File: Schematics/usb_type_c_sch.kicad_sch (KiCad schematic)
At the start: 4 parts, among them J9 USB_C_Receptacle_USB2.0_16P

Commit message: added comments, awaiting review
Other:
- note added: "USB-C for flashing firmware"
- moved on the sheet: D4, J9, R13, R14

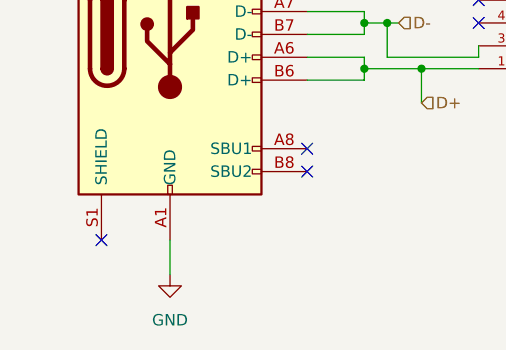
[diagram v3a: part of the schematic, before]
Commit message: fixed STLINK connector with correct pin mapping
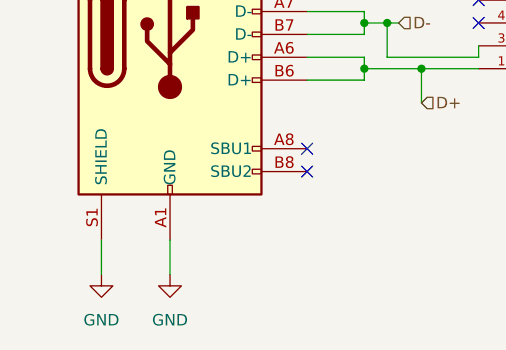
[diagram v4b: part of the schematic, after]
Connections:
- net GND: now also J9.S1 (SHIELD)
- no-connect marks 5 -> 4
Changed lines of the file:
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@@
-	)
-	(no_connect
-		(at 102.87 116.84)
 	)
 	(no_connect
@@
 		(pts
 			(xy 132.08 96.52) (xy 132.08 97.79)
+		)
+		(stroke
+			(width 0)
+			(type default)
+		)
+	)
+	(wire
+		(pts
+			(xy 102.87 120.65) (xy 102.87 116.84)
 		)
 		(stroke
@@
 		)
 	)
+	(symbol
+		(lib_id "power:GND")
+		(at 102.87 120.65 0)
+		(unit 1)
+		(body_style 1)
+		(exclude_from_sim no)
+		(in_bom yes)
+		(on_board yes)
+		(in_pos_files yes)
+		(dnp no)
+		(fields_autoplaced yes)
+		(property "Reference" "#PWR099"
+			(at 102.87 127 0)
+			(hide yes)
+			(show_name no)
+			(do_not_autoplace no)
+			(effects
+				(font
+					(size 1.27 1.27)
+				)
+			)
+		)
+		(property "Value" "GND"
+			(at 102.87 125.73 0)
+			(show_name no)
+			(do_not_autoplace no)
+			(effects
+				(font
+					(size 1.27 1.27)
+				)
+			)
+		)
+		(property "Footprint" ""
+			(at 102.87 120.65 0)
+			(hide yes)
+			(show_name no)
+			(do_not_autoplace no)
+			(effects
+				(font
+					(size 1.27 1.27)
+				)
+			)
+		)
+		(property "Datasheet" ""
+			(at 102.87 120.65 0)
+			(hide yes)
+			(show_name no)
+			(do_not_autoplace no)
+			(effects
+				(font
+					(size 1.27 1.27)
+				)
+			)
+		)
+		(property "Description" "Power symbol creates a global label with name \"GND\" , ground"
+			(at 102.87 120.65 0)
+			(hide yes)
+			(show_name no)
+			(do_not_autoplace no)
+			(effects
+				(font
+					(size 1.27 1.27)
+				)
+			)
+		)
+		(pin "1"
+		)
+		(instances
+			(project "flightcomputer2"
+				(path "/6cb3dda3-5fe8-4715-b831-354360aa3199/105f27ec-5fab-44f4-a683-69b23a7486f0"
+					(reference "#PWR099")
+					(unit 1)
+				)
+			)
+		)
+	)
